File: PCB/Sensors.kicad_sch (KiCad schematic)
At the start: 15 parts, among them U301 MMC5633NJL, U302 LSM6DSV320, U303 MS5607-02BA, U304 SAM-M8Q

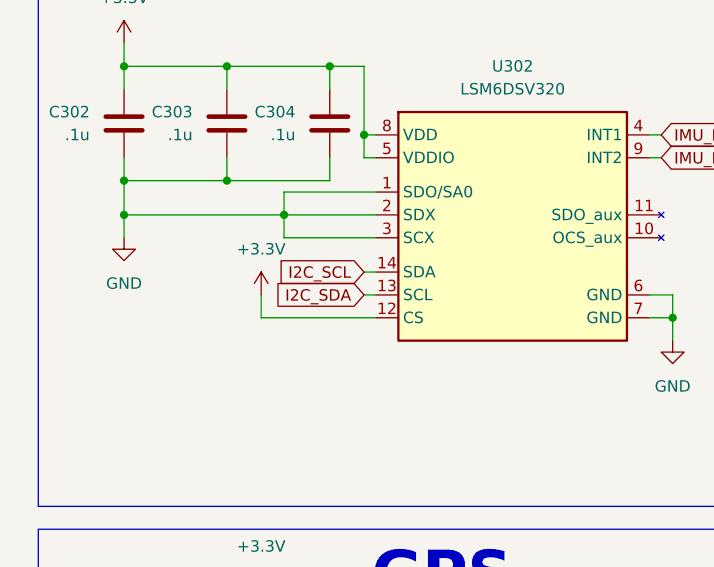
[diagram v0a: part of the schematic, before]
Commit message: Moved i2c to different set of pins
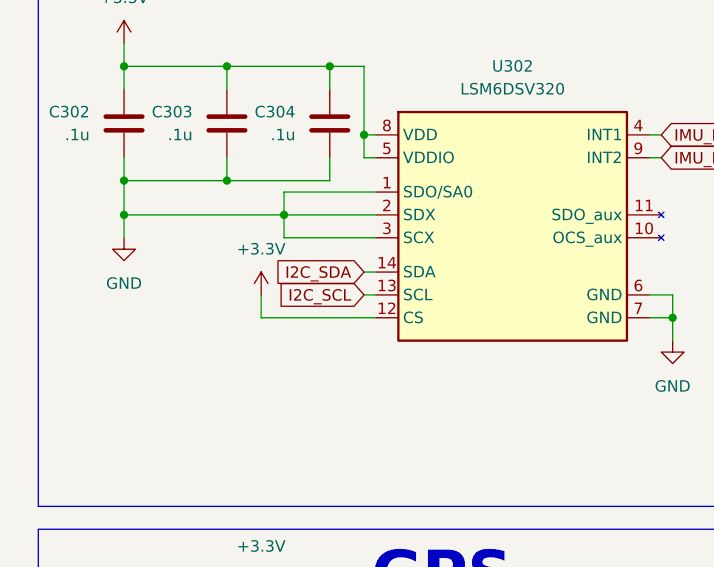
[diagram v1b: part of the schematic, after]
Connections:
- net I2C_SCL: now also U302.13 (SCL); no longer U302.14 (SDA)
- net I2C_SDA: now also U302.14 (SDA); no longer U302.13 (SCL)
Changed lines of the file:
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@@
 	(global_label "I2C_SDA"
 		(shape input)
-		(at 53.34 60.96 180)
+		(at 53.34 58.42 180)
 		(fields_autoplaced yes)
 		(effects
@@
 		)
 		(property "Intersheetrefs" "${INTERSHEET_REFS}"
-			(at 42.7348 60.96 0)
+			(at 42.7348 58.42 0)
 			(effects
 				(font
@@
 	(global_label "I2C_SCL"
 		(shape input)
-		(at 53.34 58.42 180)
+		(at 53.34 60.96 180)
 		(fields_autoplaced yes)
 		(effects
@@
 		)
 		(property "Intersheetrefs" "${INTERSHEET_REFS}"
-			(at 42.7953 58.42 0)
+			(at 42.7953 60.96 0)
 			(effects
 				(font

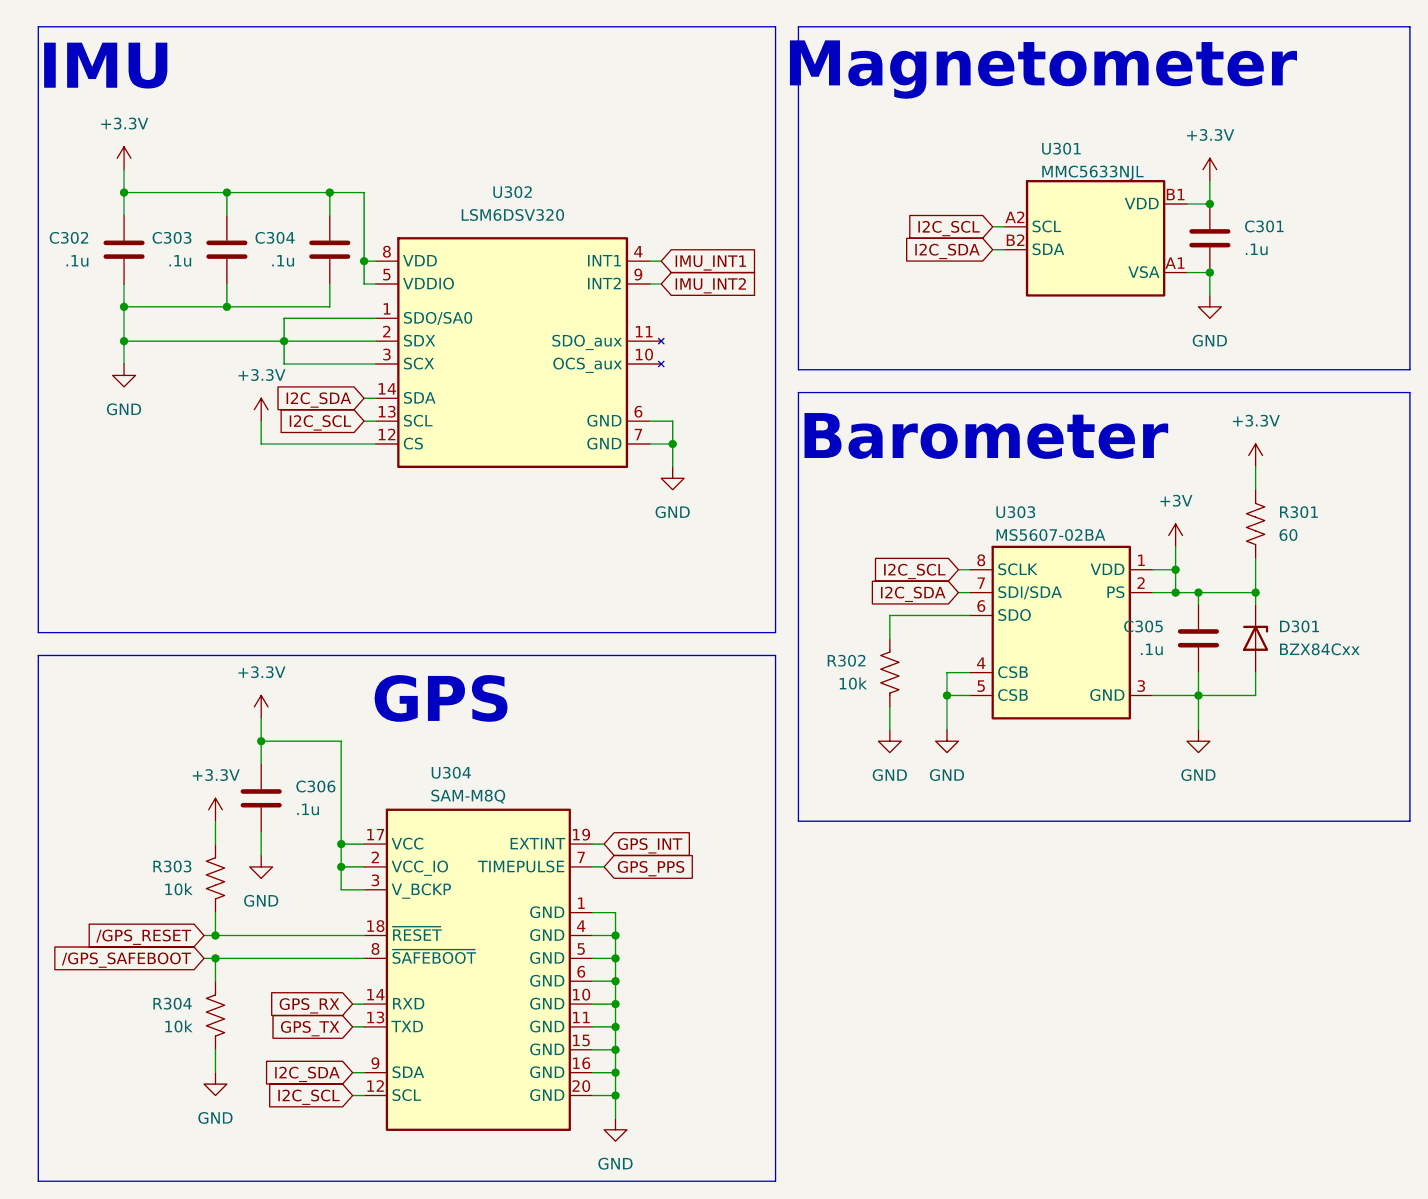
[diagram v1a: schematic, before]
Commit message: Made sensors use SPI instead of I2C Change external I2C connector to qwiic Made SWD have its own pin header
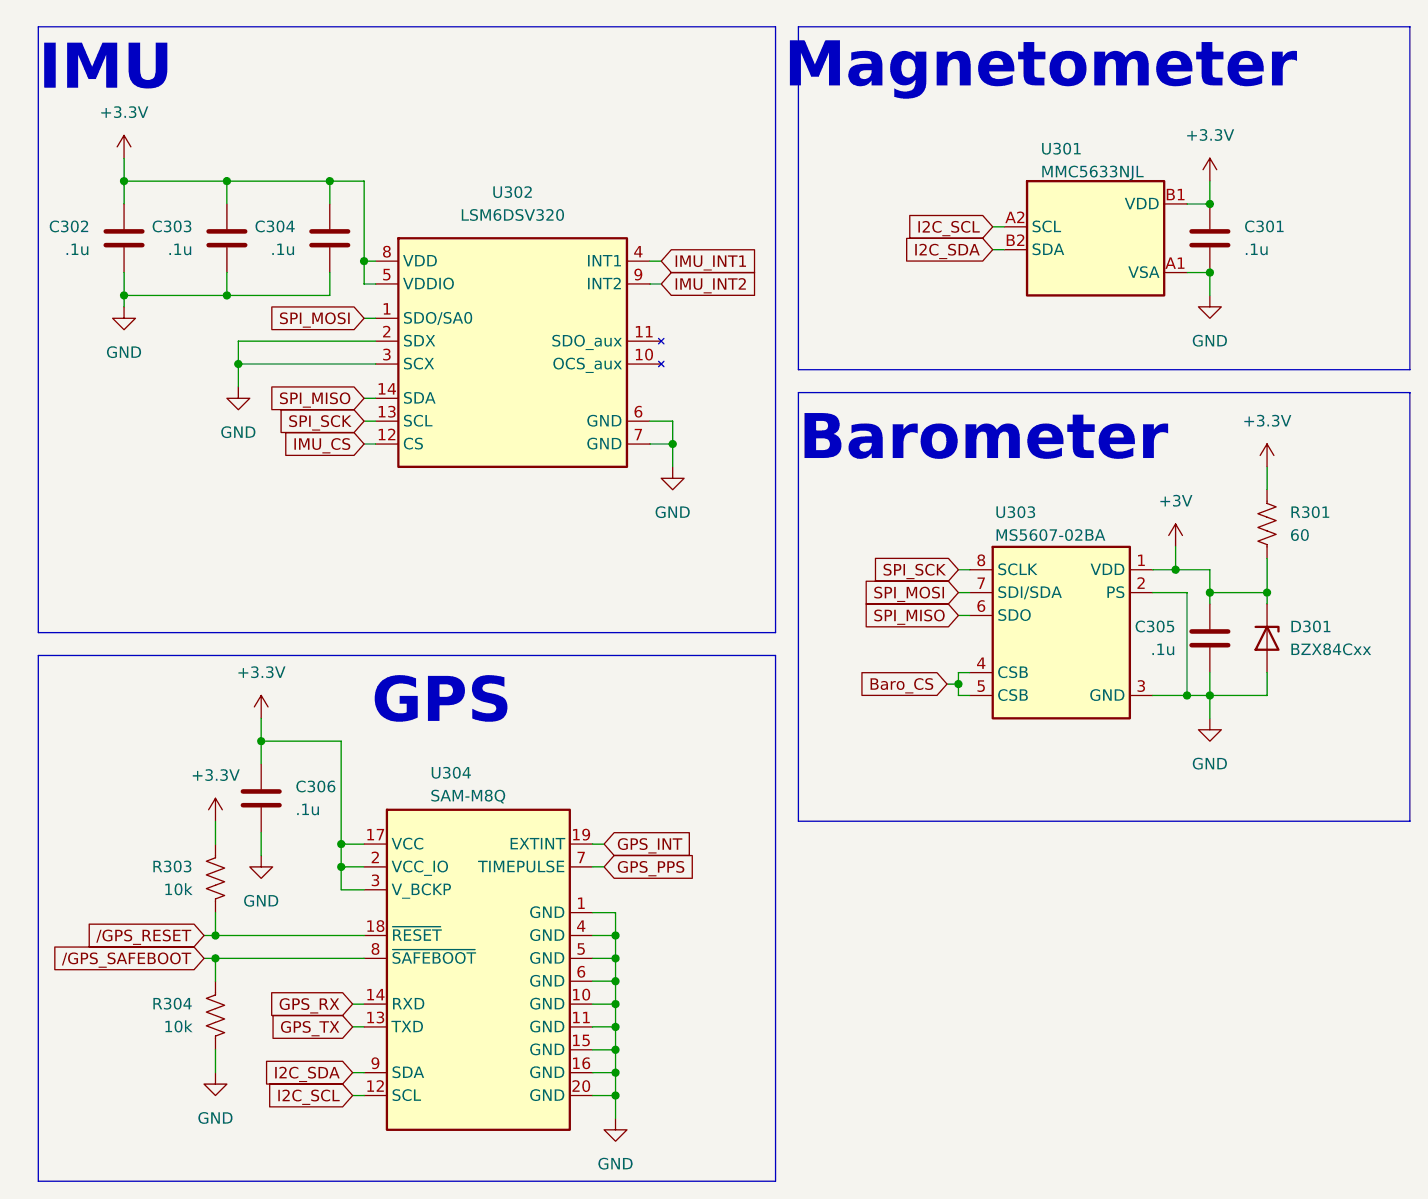
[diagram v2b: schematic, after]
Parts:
- removed R302: 10k, Resistor_SMD:R_0603_1608Metric_Pad0.98x0.95mm_HandSolder, symbol Device:R_US
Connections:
- net +3.3V: no longer U302.12 (CS)
- net +3V: no longer U303.2 (PS)
- net GND: now also U303.2 (PS); no longer U302.1 (SDO/SA0), U303.4 (CSB), U303.5 (CSB)
- net I2C_SCL: no longer U302.13 (SCL), U303.8 (SCLK)
- net I2C_SDA: no longer U302.14 (SDA), U303.7 (SDI/SDA)
- net SPI_MISO: now reaches U303.6 (SDO)
- net SPI_MISO: now also U302.14 (SDA)
- new net Baro_CS: U303.4 (CSB), U303.5 (CSB)
- new net IMU_CS: U302.12 (CS)
- new net SPI_MOSI: U302.1 (SDO/SA0), U303.7 (SDI/SDA)
- new net SPI_SCK: U302.13 (SCL), U303.8 (SCLK)
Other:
- moved on the sheet: C302, C303, C304, C305, D301, R301
